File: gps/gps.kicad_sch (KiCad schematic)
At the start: 20 parts, among them J1 Conn_01x04, J2 Conn_01x04, J3 Conn_01x04, J4 Conn_01x04, J5 Conn_01x04, U1 NEO-M8N, U2 TPS613226ADBV

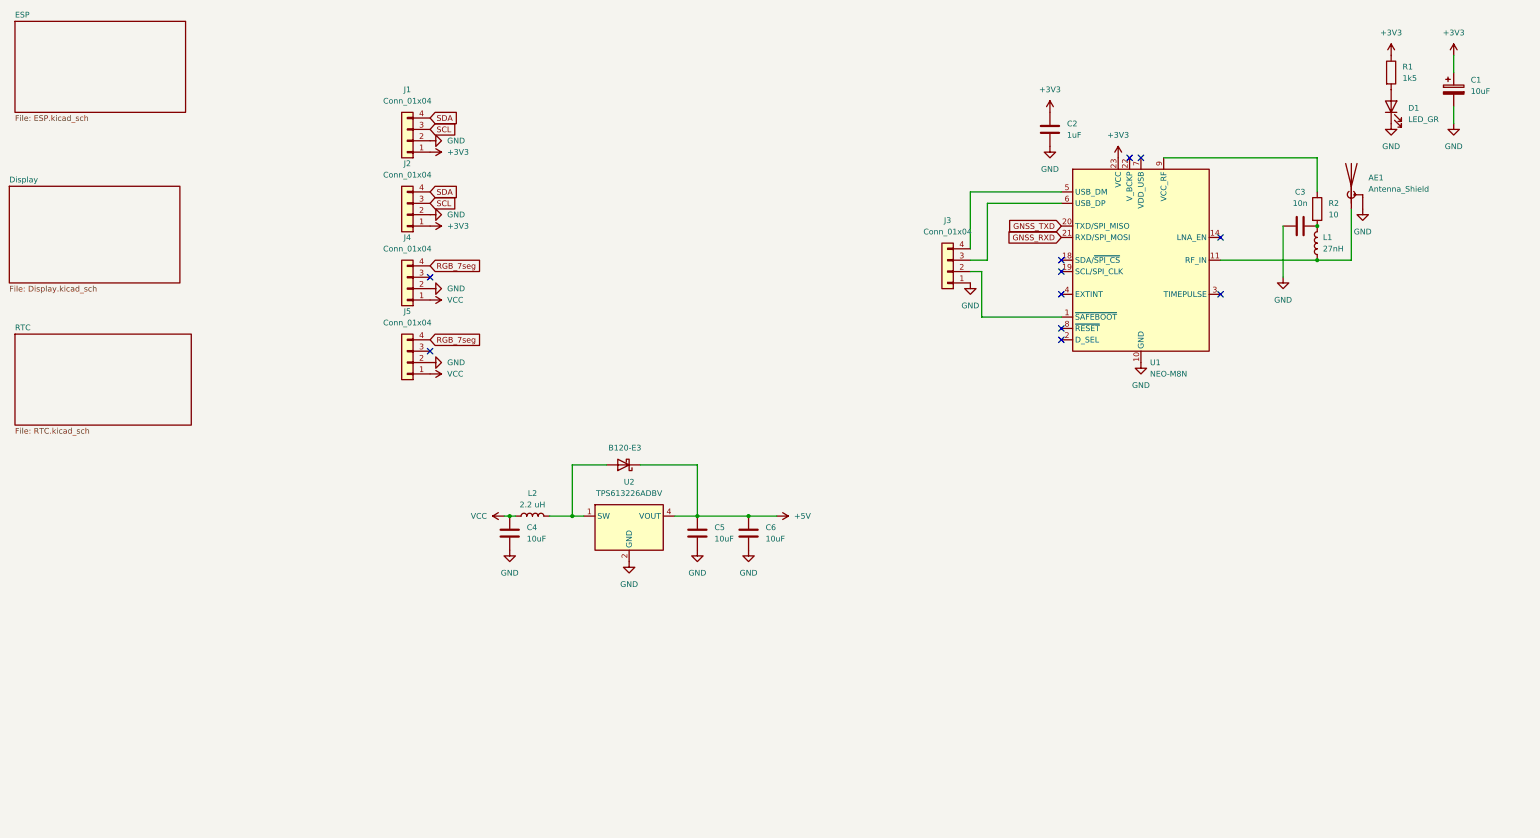
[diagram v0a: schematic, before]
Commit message: update pcb/housing
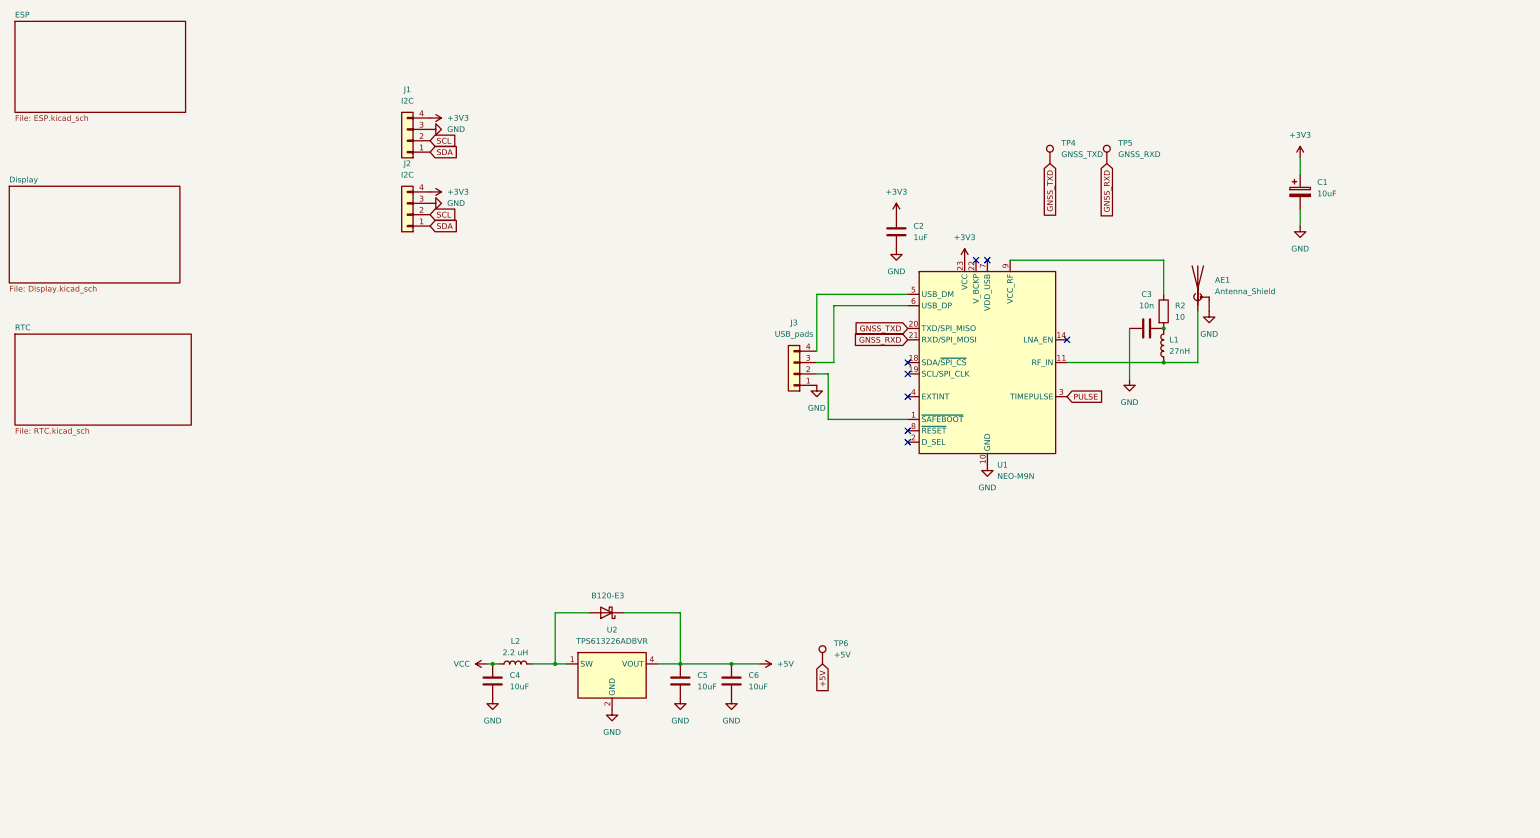
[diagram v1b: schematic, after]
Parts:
- removed D1: LED_GR, LED_SMD:LED_0805_2012Metric_Pad1.15x1.40mm_HandSolder, symbol Device:LED
- removed J4: Conn_01x04, Connector_PinHeader_2.54mm:PinHeader_1x04_P2.54mm_Vertical, symbol Connector_Generic:Conn_01x04
- removed J5: Conn_01x04, Connector_PinSocket_2.54mm:PinSocket_1x04_P2.54mm_Vertical, symbol Connector_Generic:Conn_01x04
- removed R1: 1k5, Resistor_SMD:R_0805_2012Metric_Pad1.20x1.40mm_HandSolder, symbol Device:R
- added TP4: GNSS_TXD, TestPoint:TestPoint_Loop_D1.80mm_Drill1.0mm_Beaded, symbol Connector:TestPoint
- added TP5: GNSS_RXD, TestPoint:TestPoint_Loop_D1.80mm_Drill1.0mm_Beaded, symbol Connector:TestPoint
- added TP6: +5V, TestPoint:TestPoint_Loop_D1.80mm_Drill1.0mm_Beaded, symbol Connector:TestPoint
- J1, J2: value Conn_01x04 -> I2C
- J3: value Conn_01x04 -> USB_pads
- U1: value NEO-M8N -> NEO-M9N
- U2: value TPS613226ADBV -> TPS613226ADBVR
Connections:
- net +3V3: now also J1.4 (Pin_4), J2.4 (Pin_4); no longer J1.1 (Pin_1), J2.1 (Pin_1)
- net +5V: now also TP6.1
- net GND: now also J1.3 (Pin_3), J2.3 (Pin_3); no longer J1.2 (Pin_2), J2.2 (Pin_2)
- net GNSS_RXD: now also TP5.1
- net GNSS_TXD: now also TP4.1
- net SCL: now also J1.2 (Pin_2), J2.2 (Pin_2); no longer J1.3 (Pin_3), J2.3 (Pin_3)
- net SDA: now also J1.1 (Pin_1), J2.1 (Pin_1); no longer J1.4 (Pin_4), J2.4 (Pin_4)
- net PULSE: now reaches U1.3 (TIMEPULSE)
- no-connect marks 11 -> 8
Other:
- moved on the sheet: AE1, C1, C2, C3, C4, C5, C6, J3, L1, L2, R2, U1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

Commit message: update
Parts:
- added J4: BATT, 1769:1769, symbol Connector_Generic:Conn_01x02
- added J5: ESP, Connector_PinSocket_2.54mm:PinSocket_1x02_P2.54mm_Vertical, symbol Connector_Generic:Conn_01x02
- added R1: 0R, Resistor_SMD:R_0805_2012Metric_Pad1.20x1.40mm_HandSolder, symbol Device:R
- added SW2: SW_DPDT_x2, Button_Switch_THT:MSN22AFW01, symbol Switch:SW_DPDT_x2
- J1: value I2C -> I2C_H
- J2: value I2C -> I2C_S
- U2: value TPS613226ADBVR -> TPS613222ADBVR
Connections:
- net +5V: now also R1.2; no longer C5.1, C6.1, D2.1 (K), TP6.1, U2.4 (VOUT)
- net GND: now also J4.2 (Pin_2), J5.2 (Pin_2)
- new net: C5.1, C6.1, D2.1 (K), R1.1, TP6.1, U2.4 (VOUT)
- new net: J5.1 (Pin_1), SW2.1 (A)
- new net: J4.1 (Pin_1), SW2.2 (B)
- no-connect marks 8 -> 9
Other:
- moved on the sheet: J3, R2, TP6

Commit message: PCB-update
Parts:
- removed J1: I2C_H, Connector_PinHeader_2.54mm:PinHeader_1x04_P2.54mm_Vertical, symbol Connector_Generic:Conn_01x04
- removed J2: I2C_S, Connector_PinSocket_2.54mm:PinSocket_1x04_P2.54mm_Vertical, symbol Connector_Generic:Conn_01x04
- added J1: I2C/BATT_H, Connector_PinHeader_2.54mm:PinHeader_1x07_P2.54mm_Vertical, symbol Connector_Generic:Conn_01x07
- added J2: I2C/BATT_S, Connector_PinSocket_2.54mm:PinSocket_1x07_P2.54mm_Vertical, symbol Connector_Generic:Conn_01x07
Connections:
- net +3V3: now also U1.22 (V_BCKP), J1.7 (Pin_7), J2.7 (Pin_7)
- net GND: now also J1.3 (Pin_3), J1.6 (Pin_6), J2.3 (Pin_3), J2.6 (Pin_6)
- net SCL: now also J1.5 (Pin_5), J2.5 (Pin_5)
- net SDA: now also J1.4 (Pin_4), J2.4 (Pin_4)
- net at J3.3 (Pin_3): now also U1.5 (USB_DM); no longer U1.6 (USB_DP)
- net at J3.4 (Pin_4): now also U1.6 (USB_DP); no longer U1.5 (USB_DM)
- net SW_ESP: now reaches J5.1 (Pin_1), SW2.1 (A)
- net SW_ESP: now also J1.2 (Pin_2), J2.2 (Pin_2)
- net SW_BATT: now reaches J4.1 (Pin_1), SW2.2 (B)
- net SW_BATT: now also J1.1 (Pin_1), J2.1 (Pin_1)
- no-connect marks 9 -> 8
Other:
- moved on the sheet: J5, SW2A

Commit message: tweaks
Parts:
- SW2: value SW_DPDT_x2 -> MSN22AFW01
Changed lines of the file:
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@@
 			)
 		)
-		(property "Value" "SW_DPDT_x2"
+		(property "Value" "MSN22AFW01"
 			(at 35.56 104.14 0)
 			(effects

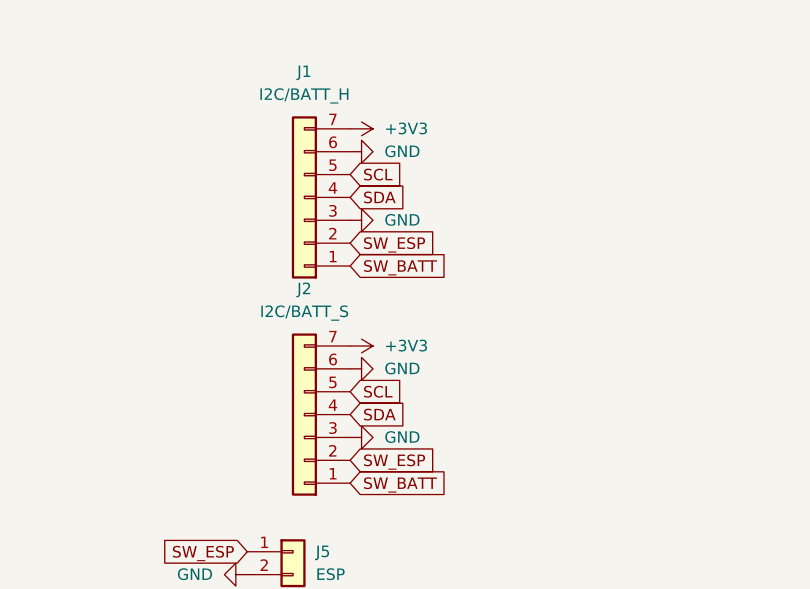
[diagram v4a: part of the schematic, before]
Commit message: added level shifters for i2C and RGB displey,
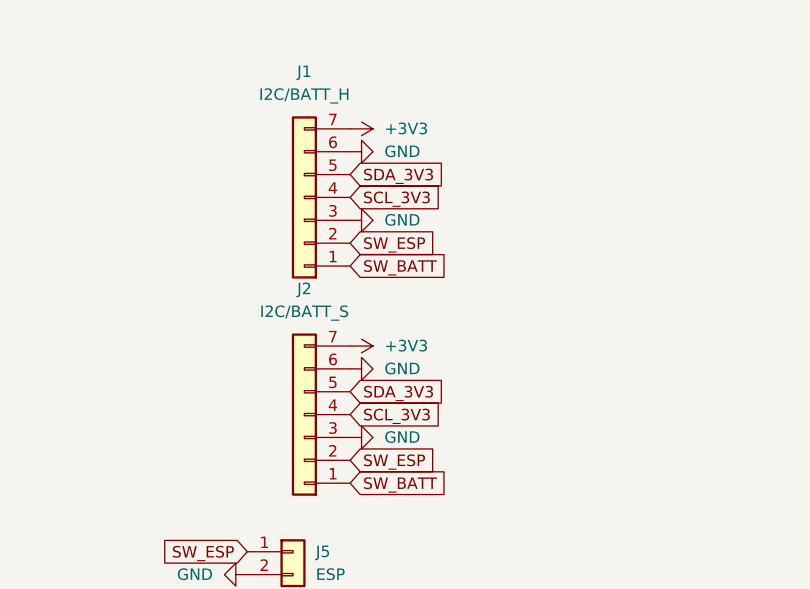
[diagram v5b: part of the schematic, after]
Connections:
- net SCL renamed SDA_3V3
- net SDA renamed SCL_3V3

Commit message: cleaned schematic
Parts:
- removed AE1: Antenna_Shield, w_conn_rf:lemo_epb00250ntn, symbol Device:Antenna_Shield
- removed C1: 10uF, Capacitor_Tantalum_SMD:CP_EIA-3528-15_AVX-H_Pad1.50x2.35mm_HandSolder, symbol Device:C_Polarized
- removed C2: 1uF, Capacitor_SMD:C_0603_1608Metric_Pad1.08x0.95mm_HandSolder, symbol Device:C
- removed C3: 10n, Capacitor_SMD:C_0805_2012Metric_Pad1.18x1.45mm_HandSolder, symbol Device:C
- removed C4, C5, C6: 10uF, Capacitor_SMD:C_0603_1608Metric_Pad1.08x0.95mm_HandSolder, symbol Device:C
- removed D2: B120-E3, Diode_SMD:D_SMA, symbol Diode:B120-E3
- removed J3: USB_pads, Connector_PinHeader_2.54mm:PinHeader_1x04_P2.54mm_Vertical, symbol Connector_Generic:Conn_01x04
- removed L1: 27nH, Inductor_SMD:L_0402_1005Metric_Pad0.77x0.64mm_HandSolder, symbol Device:L
- removed L2: 2.2 uH, Inductor_SMD:L_1008_2520Metric_Pad1.43x2.20mm_HandSolder, symbol Device:L
- removed R1: 0R, Resistor_SMD:R_0805_2012Metric_Pad1.20x1.40mm_HandSolder, symbol Device:R
- removed R2: 10, Resistor_SMD:R_1206_3216Metric_Pad1.30x1.75mm_HandSolder, symbol Device:R
- removed TP4: GNSS_TXD, TestPoint:TestPoint_Loop_D1.80mm_Drill1.0mm_Beaded, symbol Connector:TestPoint
- removed TP5: GNSS_RXD, TestPoint:TestPoint_Loop_D1.80mm_Drill1.0mm_Beaded, symbol Connector:TestPoint
- removed TP6: +5V, TestPoint:TestPoint_Loop_D1.80mm_Drill1.0mm_Beaded, symbol Connector:TestPoint
- removed U1: NEO-M9N, RF_GPS:ublox_NEO, symbol RF_GPS:NEO-M8N
- removed U2: TPS613222ADBVR, Package_TO_SOT_SMD:SOT-23-5, symbol Regulator_Switching:TPS613226ADBV
- added C10, C8, C9: 100nF, Capacitor_SMD:C_0805_2012Metric_Pad1.18x1.45mm_HandSolder, symbol Device:C
- added J12: ENC+RGB, Connector_PinSocket_2.54mm:PinSocket_1x06_P2.54mm_Vertical, symbol Connector_Generic:Conn_01x06
- added J13: ENC+RGB, Connector_PinHeader_2.54mm:PinHeader_1x06_P2.54mm_Vertical, symbol Connector_Generic:Conn_01x06
- added J7: USB_B_Micro, KiCad:USB3145301A, symbol Connector:USB_B_Micro
- added J9: USB_pads, Connector_PinSocket_2.54mm:PinSocket_1x03_P2.54mm_Vertical, symbol Connector_Generic:Conn_01x03
- added R17, R18, R19, R3, R4, R5, R6: 4k7, Resistor_SMD:R_0805_2012Metric_Pad1.20x1.40mm_HandSolder, symbol Device:R
- added RS1: 200k, Resistor_SMD:R_0805_2012Metric_Pad1.20x1.40mm_HandSolder, symbol Device:R
- added R_E1, R_E2, R_E3: 10k, Resistor_SMD:R_0805_2012Metric_Pad1.20x1.40mm_HandSolder, symbol Device:R
- added SW1: RotaryEncoder_Switch, Rotary_Encoder:RotaryEncoder_20mm_WO_mount_holes, symbol Device:RotaryEncoder_Switch
- added TP1: SDA, TestPoint:TestPoint_Loop_D1.80mm_Drill1.0mm_Beaded, symbol Connector:TestPoint
- added TP10: Jumper_MOSI, Resistor_SMD:R_0805_2012Metric_Pad1.20x1.40mm_HandSolder, symbol Connector:TestPoint_2Pole
- added TP11: Jumper_D9, Resistor_SMD:R_0805_2012Metric_Pad1.20x1.40mm_HandSolder, symbol Connector:TestPoint_2Pole
- added TP12: IO22, TestPoint:TestPoint_Loop_D1.80mm_Drill1.0mm_Beaded, symbol Connector:TestPoint
- added TP13: IO21, TestPoint:TestPoint_Loop_D1.80mm_Drill1.0mm_Beaded, symbol Connector:TestPoint
- added TP2: SCL, TestPoint:TestPoint_Loop_D1.80mm_Drill1.0mm_Beaded, symbol Connector:TestPoint
- added TP7: +3V3, TestPoint:TestPoint_Loop_D1.80mm_Drill1.0mm_Beaded, symbol Connector:TestPoint
- added TP8: DT, TestPoint:TestPoint_Loop_D1.80mm_Drill1.0mm_Beaded, symbol Connector:TestPoint
- added TP9: CLK, TestPoint:TestPoint_Loop_D1.80mm_Drill1.0mm_Beaded, symbol Connector:TestPoint
- added U10: 24C32, Package_SO:SOIC-8_3.9x4.9mm_P1.27mm, symbol Memory_EEPROM:M24C01-FMN
- added U11: SN74LV1T34DBVRG4, Package_TO_SOT_SMD:SOT-23-5, symbol Logic_LevelTranslator:SN74LV1T34DBV
- added U3: DFR0654, DFR0654:DFR0654_2, symbol DFR0654:DFR0654
- added U9: TCA39306DDFR, Package_TO_SOT_SMD:SOT-23-8, symbol shifter:TCA39306DCURQ1
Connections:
- net +3V3: now also R5.1, R6.1, R_E1.2, R_E2.2, R_E3.2, TP7.1, U3.2 (3.3V), U3.31 (3.3V), U9.2 (VREF1)
- net +5V: now also C8.2, C9.2, R17.1, R18.1, R19.1, R3.1, R4.1, RS1.1, U10.8 (VCC), U11.5 (VCC)
- net GND: now also C10.1, C8.1, C9.1, J12.1 (Pin_1), J13.1 (Pin_1), J7.5 (GND), J7.6 (Shield), SW1.C, SW1.S2, U10.4 (VSS), U10.7 (~{WC}), U11.3 (GND), U3.30 (GND), U3.34 (GND), U3.4 (GND), U9.1 (GND)
- net GNSS_RXD: now also U3.19 (D10)
- net GNSS_TXD: now also U3.20 (D11)
- net PULSE: now also U3.13 (D6)
- net SCL_3V3: now also R5.2, TP2.1, U3.29 (SCL), U3.9 (SCL), U9.3 (SCL1)
- net SDA_3V3: now also R6.2, TP1.1, U3.10 (SDA), U3.28 (SDA), U9.4 (SDA1)
- net VCC: now also J12.2 (Pin_2), J13.2 (Pin_2), U3.32 (VCC)
- new net: TP11.1, U3.12 (D7)
- new net: TP13.1, U3.21 (D12)
- new net: TP12.1, U3.22 (D13)
- new net: TP10.1, U3.7 (MOSI)
- new net: R17.2, U10.1 (E0)
- new net: R18.2, U10.2 (E1)
- new net: R19.2, U10.3 (E2)
- new net: C10.2, RS1.2, U9.7 (VREF2), U9.8 (EN)
- new net: J7.1 (VBUS), J9.3 (Pin_3)
- new net: J7.2 (D-), J9.2 (Pin_2)
- new net: J7.3 (D+), J9.1 (Pin_1)
- new net CLK: J12.6 (Pin_6), J13.6 (Pin_6), R_E2.1, SW1.A, TP9.1, U3.16 (D2)
- new net DT: J12.4 (Pin_4), J13.4 (Pin_4), R_E1.1, SW1.B, TP8.1, U3.27 (A4)
- new net RGB_3V3: J12.3 (Pin_3), J13.3 (Pin_3), TP10.2, TP11.2, U11.2 (A)
- new net RGB_5V: U11.4 (Y)
- new net SCL_5V: R4.2, U10.6 (SCL), U9.6 (SCL2)
- new net SDA_5V: R3.2, U10.5 (SDA), U9.5 (SDA2)
- new net SW: J12.5 (Pin_5), J13.5 (Pin_5), R_E3.1, SW1.S1, U3.15 (D3)
- no-connect marks 8 -> 15
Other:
- sheet ESP renamed GNSS
- removed sheet RTC
- note added: "Battery connection"
- note added: "Board connection 1/2"
- note added: "Board connection 2/2"
- note added: "D5 wired to board button"
- note added: "D9 wired to board LED"
- note added: "EEPROM"
- note added: "ESP module"
- note added: "I2C Level shifter"
- note added: "RGB 7seg Level shifter"
- note added: "Rotary encoder"
- note added: "USB Connector"
- note added: "VUSB through USB-C"
- note added: "leave A2 open"
- moved on the sheet: J1, J2, J4, J5, SW2A

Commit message: updated pdf/
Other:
- title: (none) -> GNSS_Geret
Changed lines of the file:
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@@
 	(generator_version "8.0")
 	(paper "A4")
+	(title_block
+		(title "GNSS_Geret")
+		(rev "1")
+	)
 	(junction
 		(at 101.6 120.65)
